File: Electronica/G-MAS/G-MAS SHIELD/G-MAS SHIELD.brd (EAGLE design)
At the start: 160 x 100 mm, 28 parts, among them T1-V1 2N2222, T1-V2 2N2222, T1-V3 2N2222, T1-V4 2N2222, T1-V5 2N2222

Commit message: Vibration Sensor Module
Incorpotation of the first version of the sensor module, beta, using attiny84.
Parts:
- removed B1: ARDUINO_UNO_R3_SHIELDNOLABELS, SparkFun-Boards:UNO_R3_SHIELD_NOLABELS
- removed ISP1: AVRISP-6, adafruit:AVRISP
- removed U$1: ATTINY84ATTINY84-20PU, SparkFun-IC-Microcontroller:DIP14
- added ATY: ATTINY84, SparkFun-IC-Microcontroller:DIP14
- added ATY-C1, ATY-C2: 22pF, SparkFun-Capacitors:CAP-PTH-SMALL-KIT
- added BRD-ARD1: Arduino R3, SparkFun-Boards:UNO_R3_SHIELD_NOLABELS
- added ISP-AT84: AVRISP-6, adafruit:AVRISP
- added Q1: 16MHz, special:QS
- added SV1, SV2: (no value), con-lstb:MA04-2
- T1-V1, T1-V2, T1-V3, T1-V4, T1-V5: device transistor:TO18 -> adafruit:TO92-EBC-OVAL
- moved C1-V5 186.8 mm to (9.53, 43.2), turned to 180 degrees
- moved R1-V5 176.9 mm to (23.5, 36.2), turned to 90 degrees
- moved D1-V5 174.7 mm to (12.7, 40.0), turned to 180 degrees
- moved T1-V5 164.3 mm to (17.1, 41.9), turned to 180 degrees
- moved JST-V5 157.5 mm to (3.81, 41.9), turned to 90 degrees
- moved C1-V4 142.2 mm to (9.53, 34.3), turned to 180 degrees
- moved R1-V4 140.5 mm to (21.0, 36.2), turned to 90 degrees
- moved C1-V3 133.5 mm to (10.2, 25.4), turned to 180 degrees
- moved R1-V3 131.2 mm to (21.6, 26.0), turned to 90 degrees
- moved D1-V4 130.3 mm to (12.7, 31.1), turned to 180 degrees
- moved T1-V4 126.2 mm to (15.9, 33.0), turned to 180 degrees
- moved D1-V3 121.5 mm to (12.7, 22.2), turned to 180 degrees
- moved JST-V4 113.7 mm to (3.81, 33.0), turned to 90 degrees
- moved T1-V3 111.2 mm to (17.8, 24.1), turned to 180 degrees
- moved JST-V3 104.2 mm to (3.81, 24.1), turned to 90 degrees
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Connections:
- new net ATY-X1: ATY-C1.2, ATY.2, Q1.1
- new net ATY-X2: ATY-C2.2, ATY.3, Q1.2
- new net CM1-TDR: ATY.5, BRD-ARD1.D3
- new net ECH1: ATY.11, SV2.3
- new net ECH2: ATY.12, SV2.4
- new net ECH3: ATY.7, ISP-AT84.4, SV1.3
- new net ECH4: ATY.8, ISP-AT84.1, SV1.4
- new net RS/CM1-RDS: ATY.4, BRD-ARD1.D2, ISP-AT84.5
- new net TRI1: ATY.10, SV2.5
- new net TRI2: ATY.13, SV2.6
- new net TRI3: ATY.6, SV1.5
- new net TRI4: ATY.9, ISP-AT84.3, SV1.6
- net 5V: now also ATY.1, BRD-ARD1.5V, ISP-AT84.2, SV1.7, SV1.8, SV2.7, SV2.8; no longer B1.5V, ISP1.2, U$1.1
- net CN-V1: now also BRD-ARD1.D11
- net CN-V2: now also BRD-ARD1.D10
- net CN-V3: now also BRD-ARD1.D9
- net CN-V4: now also BRD-ARD1.D6
- net GND: now also ATY-C1.1, ATY-C2.1, ATY.14, BRD-ARD1.GND@0, ISP-AT84.6, SV1.1, SV1.2, SV2.1, SV2.2, T1-V1.E, T1-V2.E, T1-V3.E, T1-V4.E, T1-V5.E; no longer B1.GND@0, ISP1.6, T1-V1.1, T1-V2.1, T1-V3.1, T1-V4.1, T1-V5.1, U$1.14
- net N$1: now also T1-V1.C; no longer T1-V1.3
- net N$10: now also T1-V5.B; no longer T1-V5.2
- net N$2: now also T1-V2.C; no longer T1-V2.3
- net N$3: now also T1-V1.B; no longer T1-V1.2
- net N$4: now also T1-V2.B; no longer T1-V2.2
- net N$5: now also T1-V3.C; no longer T1-V3.3
- net N$6: now also T1-V3.B; no longer T1-V3.2
- net N$7: now also T1-V4.C; no longer T1-V4.3
- net N$8: now also T1-V4.B; no longer T1-V4.2
- net N$9: now also T1-V5.C; no longer T1-V5.3
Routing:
- net 5V: track 0.00 -> 119.1 mm
- net 3.3V: track 0.00 -> 99.4 mm
- net RS/CM1-RDS: track 0.00 -> 54.9 mm
- net TRI1: track 0.00 -> 52.6 mm
- net ECH1: track 0.00 -> 46.0 mm
- net TRI4: track 0.00 -> 43.8 mm
- net ECH3: track 0.00 -> 36.6 mm
- net ECH4: track 0.00 -> 34.6 mm
- net CM1-TDR: track 0.00 -> 30.1 mm
- net ATY-X2: track 0.00 -> 29.6 mm
- net ECH2: track 0.00 -> 29.6 mm
- net TRI2: track 0.00 -> 29.6 mm
- net ATY-X1: track 0.00 -> 24.9 mm
- net N$1: track 0.00 -> 22.6 mm
- net N$7: track 0.00 -> 22.2 mm
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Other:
- board size 160 x 100 mm -> 160 x 53 mm

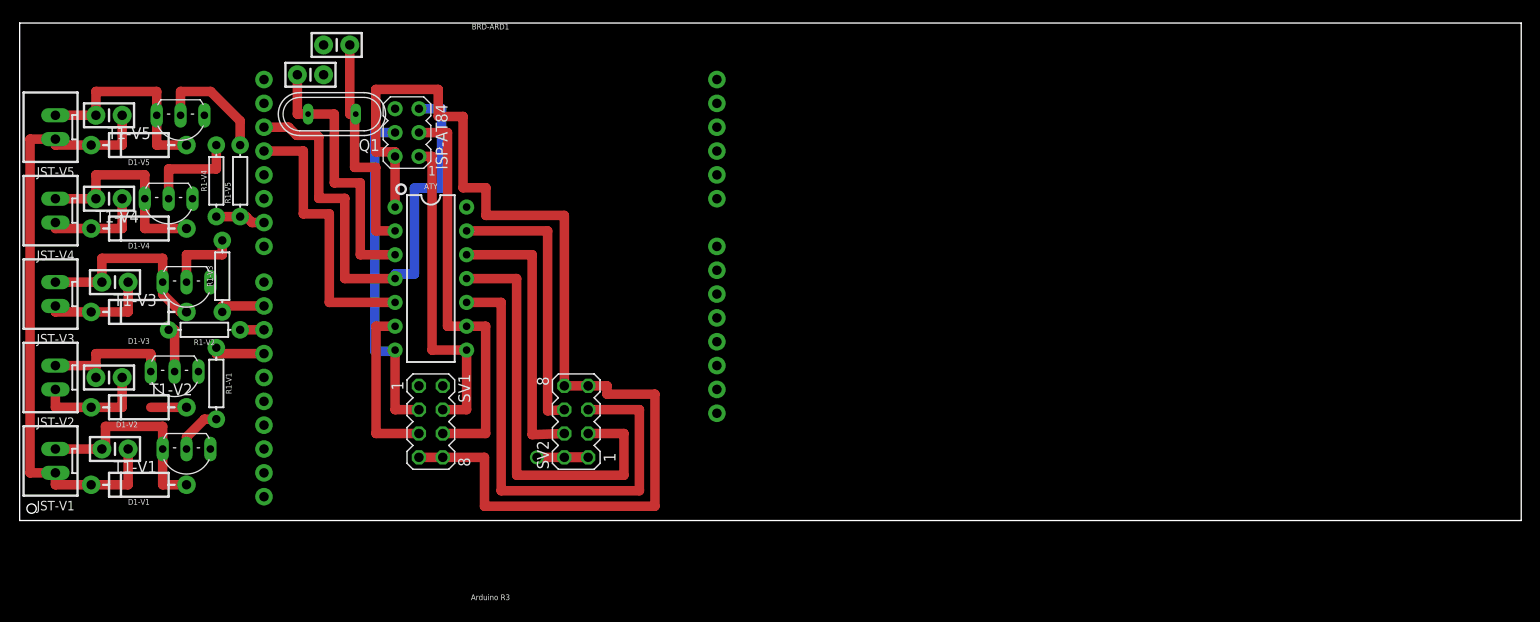
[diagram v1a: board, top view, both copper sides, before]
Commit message: V1
Incorporacion de MicroSD
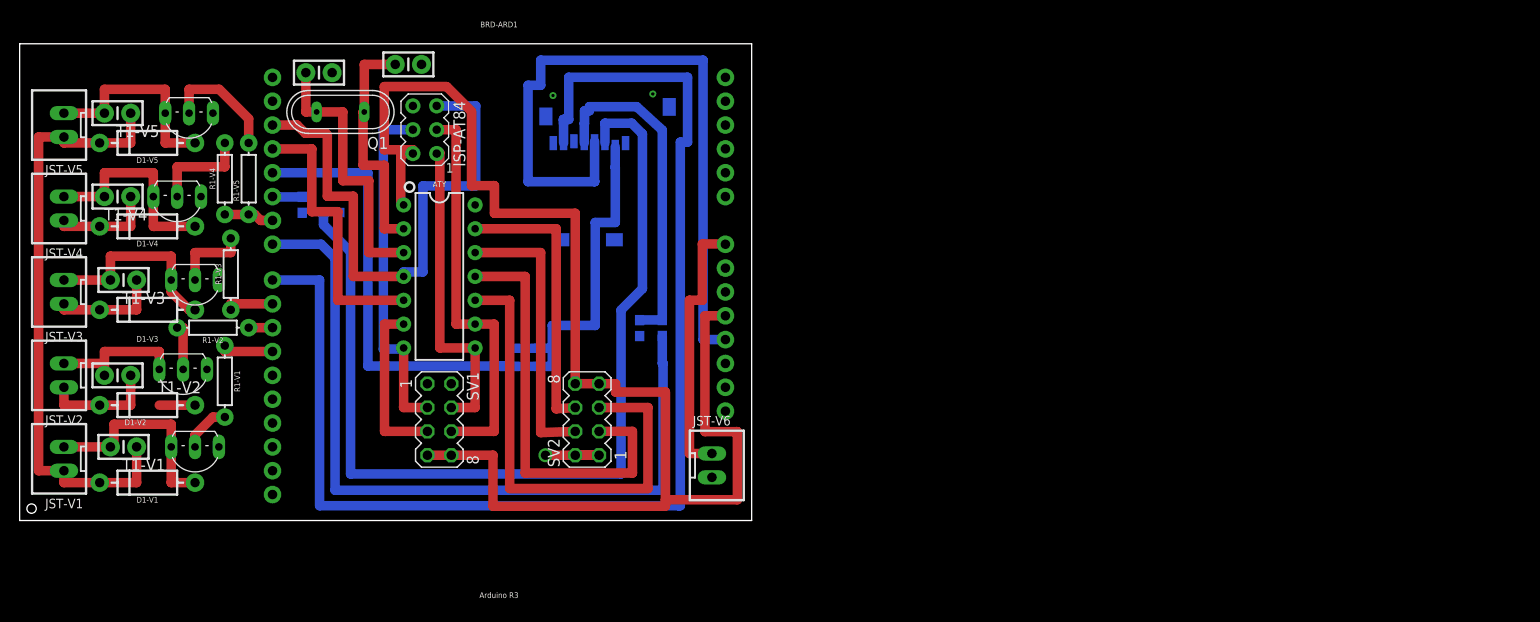
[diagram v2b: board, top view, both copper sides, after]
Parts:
- added J1: MICRO-SD_CARD_SOCKET, SparkFun-Connectors:MICRO-SD-SOCKET
- added JST-V6: JST-V1, Rembrandt Electronics - JST XH Connectors v1-0:JST-XH-02-PACKAGE-LONG-PAD
- added SD-R1, SD-R3, SD-R5: 1.8k, SparkFun-Resistors:0603
- added SD-R2, SD-R4, SD-R6: 3.3k, SparkFun-Resistors:0603
- moved ATY-C1 7.91 mm to (41.4, 48.6), turned to 180 degrees
- moved ISP-AT84 1.92 mm to (43.2, 41.6)
- moved SV2 1.18 mm to (60.5, 10.8)
- moved ATY-C2 0.94 mm to (31.9, 47.7)
- moved T1-V5 0.94 mm to (18.1, 42.1)
- moved ATY 0.94 mm to (44.7, 26.0)
- moved BRD-ARD1 0.94 mm to (51.1, 23.1)
- moved D1-V2 0.94 mm to (13.6, 12.3)
- moved D1-V4 0.94 mm to (13.6, 31.3)
- moved R1-V2 0.94 mm to (20.6, 20.5)
- moved R1-V3 0.94 mm to (22.5, 26.3)
- moved D1-V1 0.94 mm to (13.6, 4.04)
- moved JST-V5 0.94 mm to (4.72, 42.1)
- moved R1-V1 0.94 mm to (21.9, 14.8)
- moved SV1 0.94 mm to (44.7, 10.8)
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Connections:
- new net 3V3: BRD-ARD1.3.3V, J1.VCC
- new net N$11: J1.SCLK, SD-R1.1, SD-R2.2
- new net N$12: J1.CS, SD-R3.1, SD-R4.2
- new net N$13: J1.DI, SD-R5.1, SD-R6.2
- new net SD-CS: BRD-ARD1.D4, SD-R3.2
- new net SD-MISO: BRD-ARD1.D8, J1.DO
- new net SD-MOSI: BRD-ARD1.D5, SD-R5.2
- new net SD-SCK: BRD-ARD1.D7, SD-R1.2
- new net VIN: BRD-ARD1.VIN, JST-V6.1
- net GND: now also BRD-ARD1.GND@1, BRD-ARD1.GND@2, J1.GND, J1.GND1, J1.GND3, JST-V6.2, SD-R2.1, SD-R4.1, SD-R6.1
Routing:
- net SD-MISO: track 0.00 -> 134.7 mm
- net N$13: track 0.00 -> 101.7 mm
- net SD-SCK: track 0.00 -> 83.5 mm
- net 3V3: track 0.00 -> 75.2 mm
- net SD-CS: track 0.00 -> 47.4 mm
- net N$11: track 0.00 -> 35.8 mm
- net 5V: track 119.1 -> 154.0 mm
- net N$12: track 0.00 -> 33.8 mm
- net VIN: track 0.00 -> 28.6 mm
- net RS/CM1-RDS: track 54.9 -> 59.5 mm
- net SD-MOSI: track 0.00 -> 3.20 mm
- net ECH3: track 36.6 -> 37.7 mm
- net TRI4: track 43.8 -> 42.8 mm
- net ECH4: track 34.6 -> 33.8 mm
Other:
- board size 160 x 53 mm -> 78 x 50.8 mm
